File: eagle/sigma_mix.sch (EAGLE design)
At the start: 155 parts, among them J1 POWER_JACK, J2 RCA_JACK_CUI, J3 RCA_JACK_CUI, J4 RCA_JACK_CUI, J5 RCA_JACK_CUI, J6 RCA_JACK_X2_CUI, J7 RCA_JACK_X2_CUI, J8 RCA_JACK_X2_CUI, J9 RCA_JACK_X2_CUI, U1 MCP1726, U2 MCP73871, U3 ADM811TARTZ-REEL7, U4 ADAU1701JSTZ, U5 ADAU1701JSTZ, X1 2510-, X2 2510-, X3 12.288MHz, X4 12.288MHz

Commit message: Release ver0.2.
Fixed some bugs of issue.
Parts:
- removed C1, C4, C5: 4.7uF, rcl:C-EUC2012
- removed C2: 1000pF, rcl:C-EUC2012
- removed C6: 1uF, rcl:C-EUC2012
- removed CN1: (no value), adafruit:JST_2PIN-SMT-RA
- removed LED1, LED2, LED3: (no value), led:LEDCHIPLED_0603
- removed R2, R3, R4, R6: 1k, SparkFun:RESISTOR0603-RES
- removed R5: 10k, SparkFun:RESISTOR0603-RES
- removed R7: 100k, SparkFun:RESISTOR0603-RES
- removed U1: MCP1726, tkrworks:MCP1725
- removed X3, X4: 12.288MHz, tkrworks2:ABMXX-XXMHZ-XX-X-X-X
- added JP5: SWD Interface, con-3m:2520-
- added JP6: USBi, con-3m:2510-
- added JP7: (no value), pinhead:PINHD-2X5
- C18, C19, C24, C25: device rcl:C-USC0805 -> rcl:CPOL-USR/2012-12R
- C3: value 4.7uF -> 10uF; device rcl:C-EUC2012 -> rcl:CPOL-USR/2012-12R
- C40, C41: value 0.1uF -> 56nF
- C42, C43: value 10uF -> 3.3nF
- R1: value 10k -> 100k
- T1, T2: device transistor:-PNP-SOT23-EBC -> zetex:PNPSOT23
- U2: value MCP73871 -> (none); device tkrworks:MCP73871 -> tkrworks:MIC39100
- X1, X2: value 2510- -> 12.288MHz; device con-3m:2510- -> tkrworks2:ABMXX-XXMHZ-XX-X-X-X
- renumbered IC1 to U6, S1 to SW3, S2 to SW4, SV1 to JP4, SV2 to JP3
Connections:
- removed net DEBUG_CLOCK: U6.PF1, X1-8.KL
- removed net DEBUG_DATA: U6.PF0, X1-7.KL
- removed net N$13: C2.1, U1.6_CDELAY
- removed net N$14: R7.1, U1.5PWRGND
- removed net N$17: R2.2, U2./PG
- removed net N$18: R3.2, U2.STAT2
- removed net N$23: LED1.C, R2.1
- removed net N$25: LED2.C, R3.1
- removed net N$27: LED3.C, R4.1
- removed net N$29: R4.2, U2.STAT1/LBO
- removed net N$30: R1.2, U2.THERM
- removed net N$31: R5.2, U2.PROG3
- removed net N$32: R6.2, U2.PROG1
- removed net N$5: C22.1, C24.1, C26.1, T1.C, U4A.DVDD, U4A.DVDD_2
- removed net VBAT: C4.1, CN1.2, U2.VBAT0, U2.VBAT1, U2.VBAT2
- removed net VBUS: C5.1, J1.PWR, LED1.A, LED2.A, LED3.A, U2.CE, U2.IN0, U2.IN1, U2.VPCC
- new net 5V-SUPPLY: JP5-19.KL
- new net DVDD: C22.1, C24.+, C26.1, T1.C, U4A.DVDD, U4A.DVDD_2
- new net FLG: R1.2, U2.FLG
- new net SWCLK: JP5-9.KL, U6.PF1
- new net SWDIO: JP5-7.KL, U6.PF0
- new net SWO: JP5-13.KL
- new net VTREF: JP5-1.KL
- net *RESET: now also JP5-15.KL; no longer X1-4.KL
- net BRD_RESET: now also JP6-6.KL; no longer X2-6.KL
- net GND: now also C18.-, C19.-, C24.-, C25.-, C3.-, JP5-10.KL, JP5-12.KL, JP5-14.KL, JP5-16.KL, JP5-18.KL, JP5-20.KL, JP5-4.KL, JP5-6.KL, JP5-8.KL, JP6-10.KL, JP7.10, JP7.2, JP7.4, JP7.6, JP7.8, U2.GND@1, U2.GND@2, U2.GND@3, U2.GND@4; no longer C1.2, C18.2, C19.2, C2.2, C24.2, C25.2, C3.2, C4.2, C5.2, C6.2, CN1.1, R1.1, R5.1, R6.1, U1.4_GND, U2./TE, U2.EP, U2.PROG2, U2.SEL, U2.VSS0, U2.VSS1, X1-10.KL, X2-10.KL
- net MCLKI_1: now also X1.P$2; no longer X3.P$2
- net MCLKI_2: now also X2.P$2; no longer X4.P$2
- net N$11: now also JP6-2.KL; no longer X2-2.KL
- net N$37: now also C25.+; no longer C25.1
- net N$43: now also X2.P$1; no longer X4.P$1
- net N$9: now also X1.P$1; no longer X3.P$1
- net PSW: now also U2.EN; no longer U1.3_SHDN
- net SCL: now also JP6-1.KL; no longer X2-1.KL
- net SDA: now also JP6-3.KL; no longer X2-3.KL
- net VDD: now also C18.+, C19.+, C3.+, JP7.1, JP7.3, JP7.5, JP7.7, JP7.9, U2.OUT; no longer C18.1, C19.1, C6.1, R7.2, U1.7_SENSE, U1.8_VOUT, X1-9.KL
- net VIN: now also J1.PWR, R1.1, U2.IN; no longer C1.1, C3.1, U1.1_VIN, U1.2_VIN, U2.OUT0, U2.OUT1

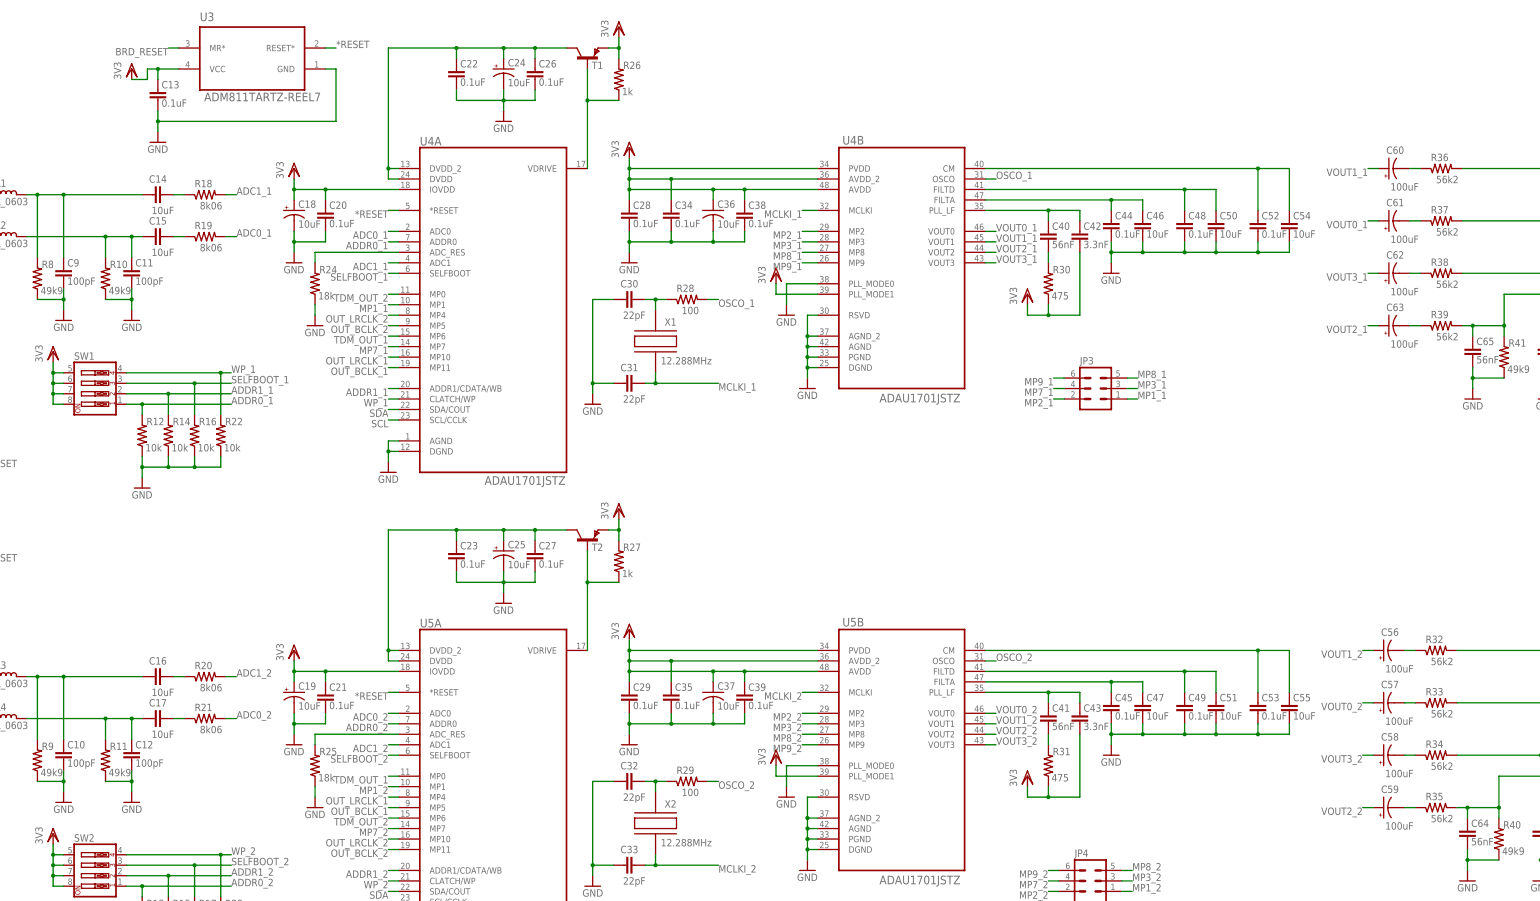
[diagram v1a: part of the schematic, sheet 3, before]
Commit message: Release ver0.3.
Fixed the issue #11, #12, #13.
Fixed some silk positions.
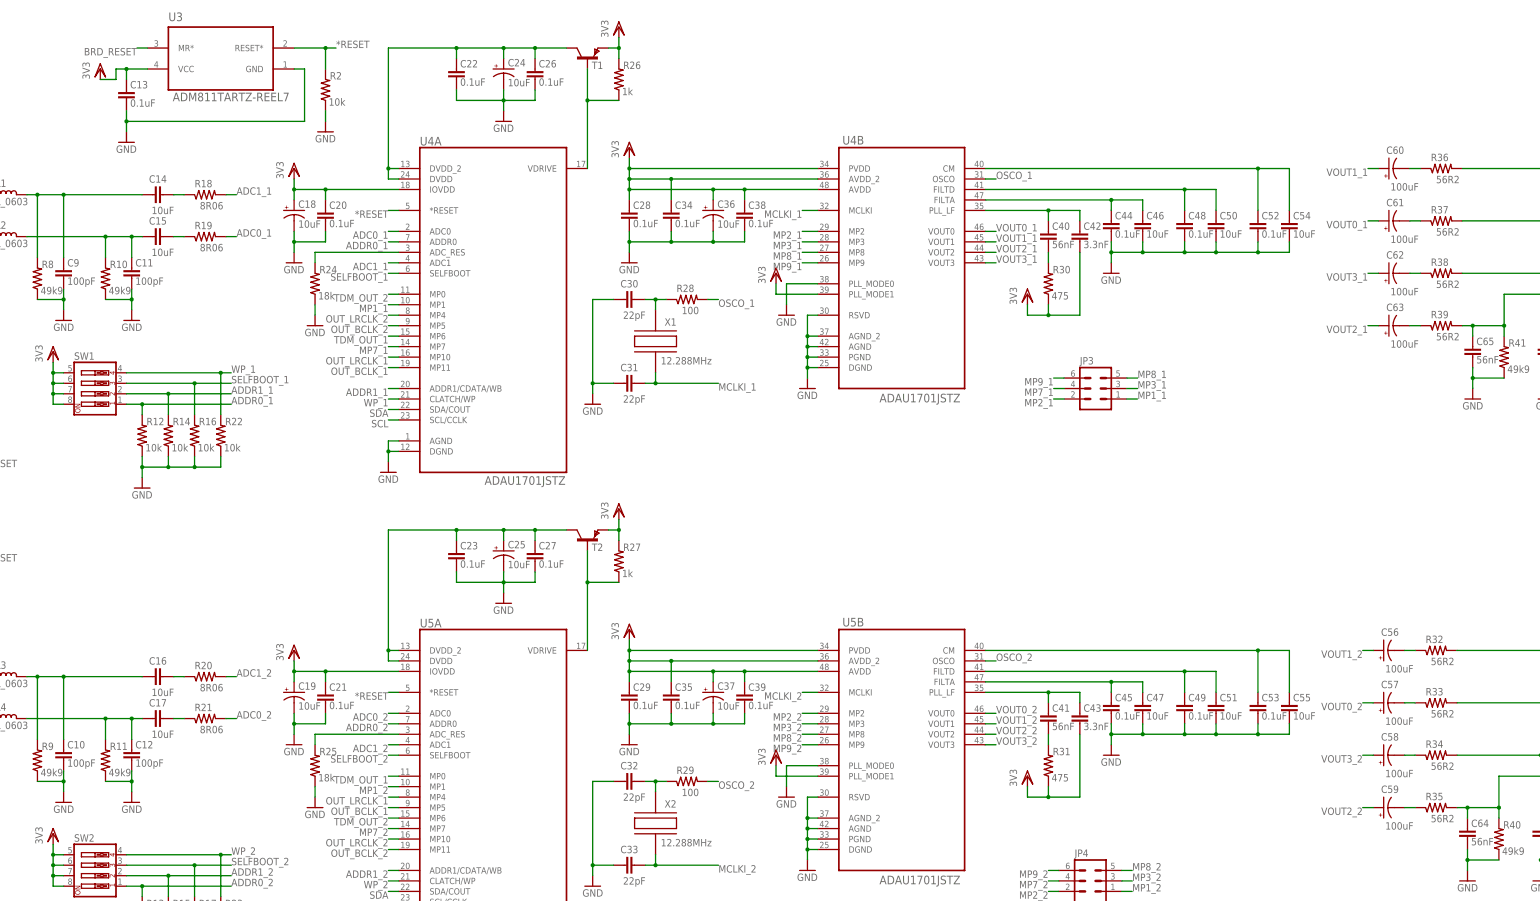
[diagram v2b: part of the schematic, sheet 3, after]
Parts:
- added R2: 10k, SparkFun:RESISTOR0603-RES
- C36, C37: device rcl:C-USC0805 -> rcl:CPOL-USR/2012-12R
- R18, R19, R20, R21: value 8k06 -> 8R06
- R32, R33, R34, R35, R36, R37, R38, R39: value 56k2 -> 56R2
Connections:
- net *RESET: now also R2.2
- net GND: now also C36.-, C37.-, R2.1; no longer C36.2, C37.2
- net VDD: now also C36.+, C37.+; no longer C36.1, C37.1
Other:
- moved on the sheet: C13, U3

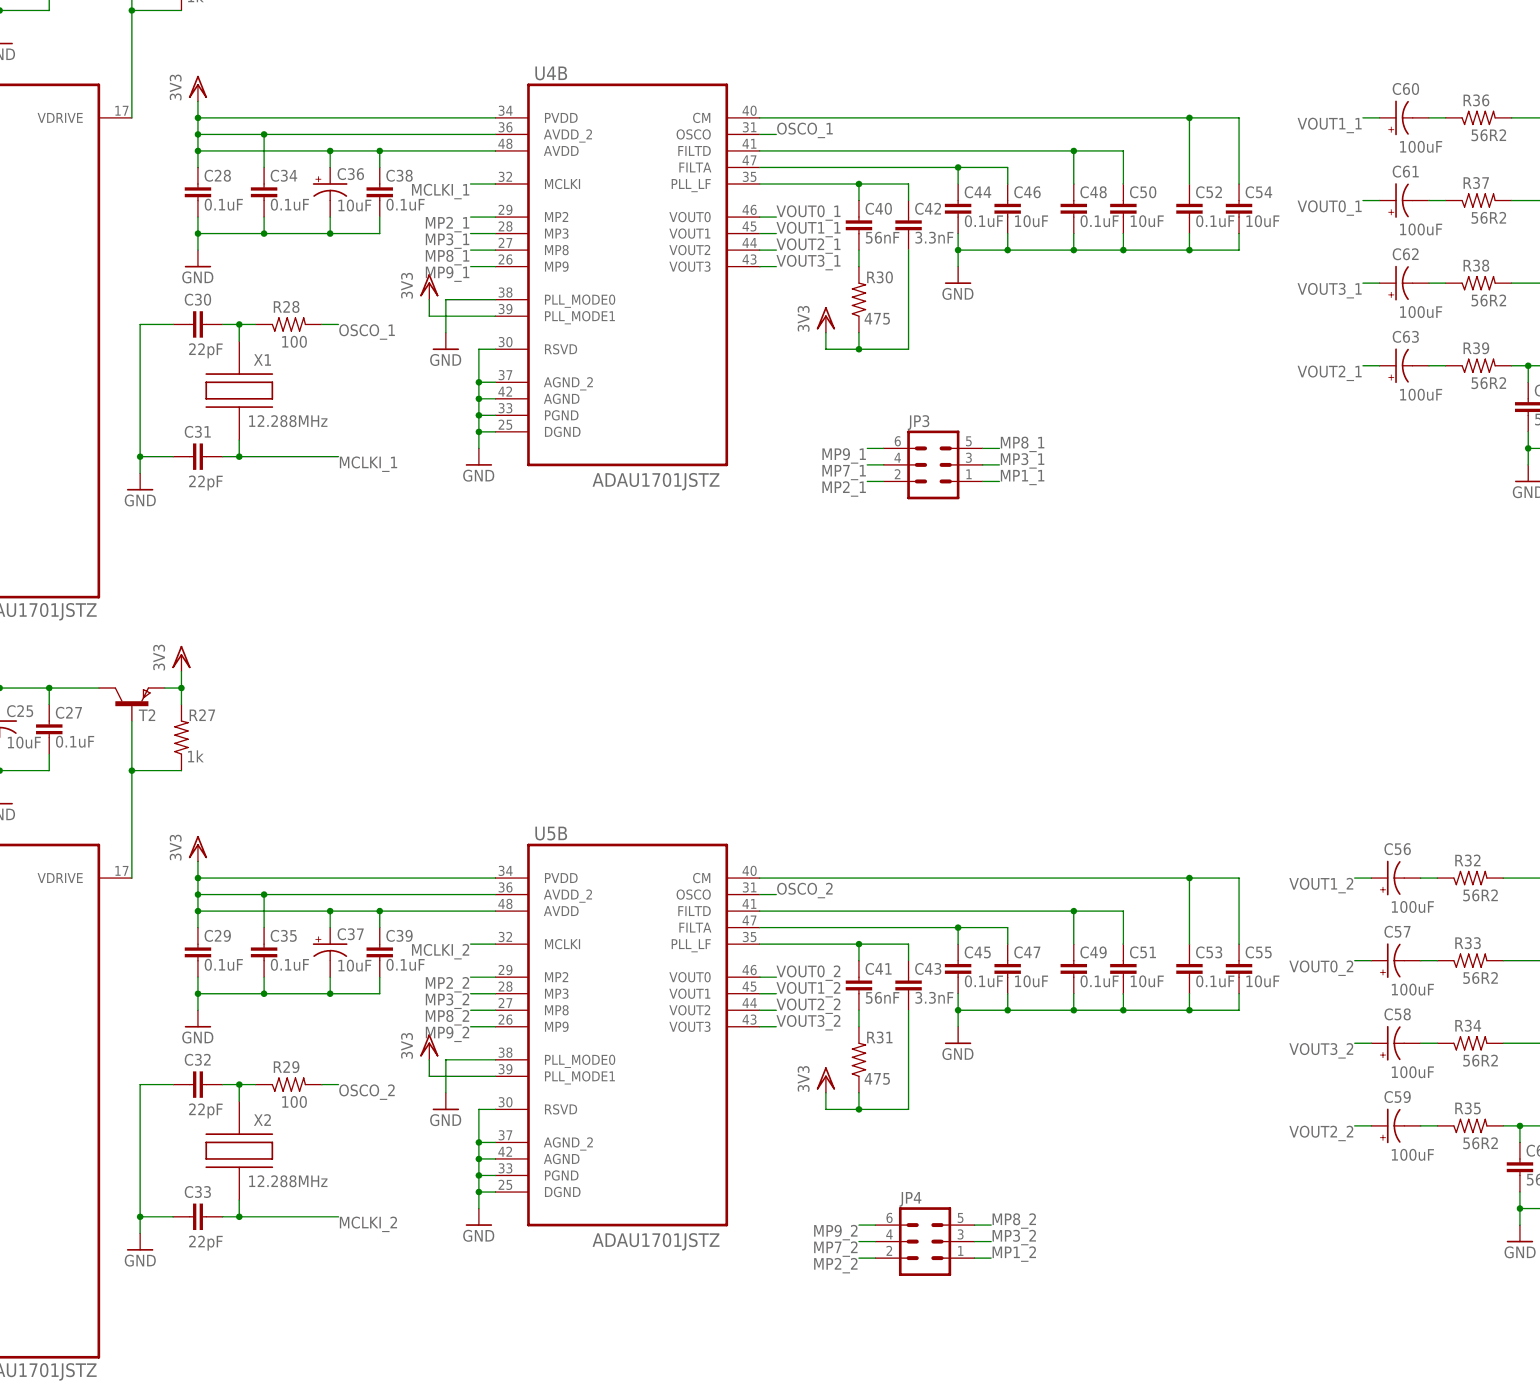
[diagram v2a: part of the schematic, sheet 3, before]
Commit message: Reseale ver 0.4.
Fxed the issues #14, #15, #16 and #18.
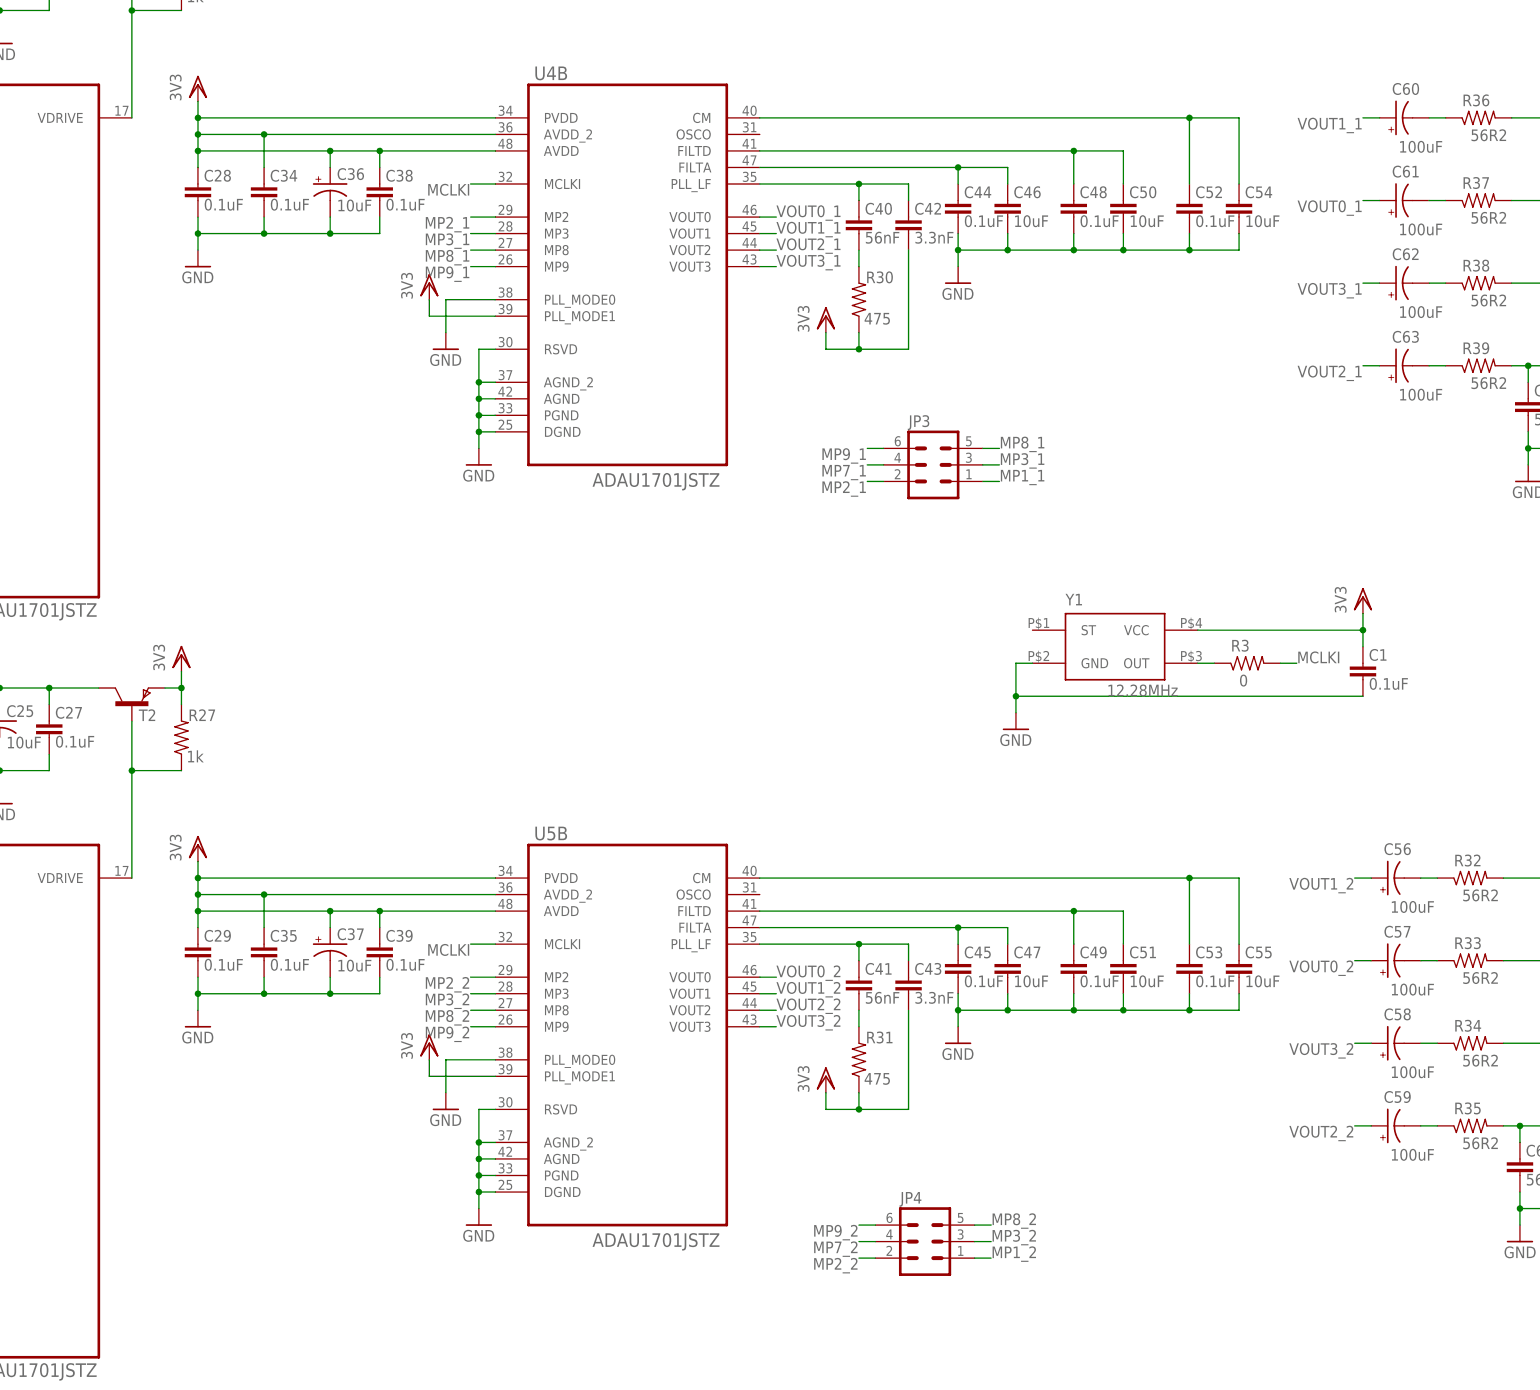
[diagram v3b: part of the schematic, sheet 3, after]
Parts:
- removed C30, C31, C32, C33: 22pF, rcl:C-EUC2012
- removed R28, R29: 100, SparkFun:RESISTOR0603-RES
- removed X1, X2: 12.288MHz, tkrworks2:ABMXX-XXMHZ-XX-X-X-X
- added C1: 0.1uF, rcl:C-EUC2012
- added C2: 1uF, rcl:C-EUC2012
- added R3: 0, SparkFun:RESISTOR0603-RES
- added Y1: 12.28MHz, tkrworks2:XTAL-OSC
- JP2, JP7: device pinhead:PINHD-2X5 -> pinhead:PINHD-2X6
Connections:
- removed net MCLKI_1: C31.1, U4B.MCLKI, X1.P$2
- removed net MCLKI_2: C33.1, U5B.MCLKI, X2.P$2
- removed net N$43: C32.1, R29.1, X2.P$1
- removed net N$9: C30.1, R28.1, X1.P$1
- removed net OSCO_1: R28.2, U4B.OSCO
- removed net OSCO_2: R29.2, U5B.OSCO
- removed net VTREF: JP5-1.KL
- new net MCLKI: R3.2, U4B.MCLKI, U5B.MCLKI
- new net N$5: R3.1, Y1.OUT
- net *RESET: no longer JP5-15.KL
- net BRD_RESET: now also JP5-15.KL
- net GND: now also C1.2, C2.2, JP2.12, JP7.12, Y1.GND; no longer C30.2, C31.2, C32.2, C33.2
- net SWCLK: now also JP5-7.KL; no longer JP5-9.KL
- net SWDIO: now also JP5-9.KL; no longer JP5-7.KL
- net VDD: now also C1.1, JP2.11, JP5-1.KL, JP7.11, Y1.VCC
- net VIN: now also C2.1
